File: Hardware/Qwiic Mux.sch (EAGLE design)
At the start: 77 parts, among them J1 SMD, J10 SMD, J11 PTH, J12 PTH, J13 PTH, J14 PTH, J2 SMD, J23 SMD, J24 SMD, J25 SMD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

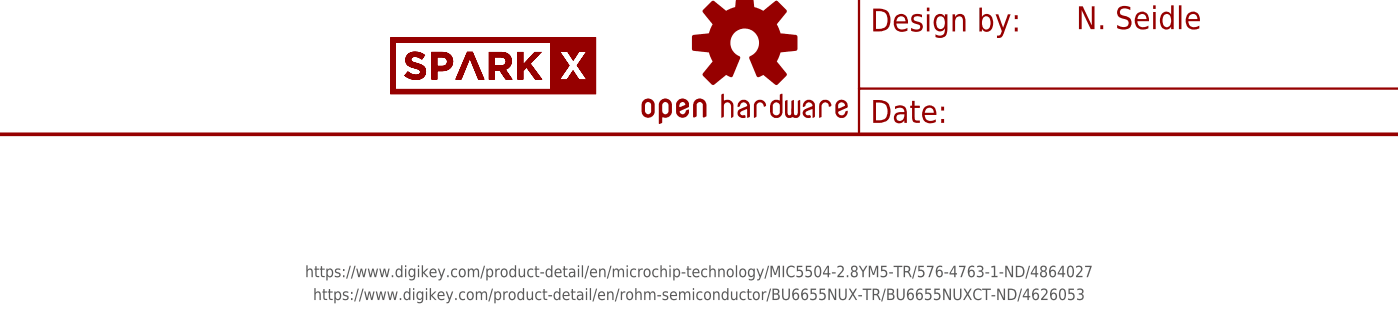
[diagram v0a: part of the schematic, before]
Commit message: Adding example firmware
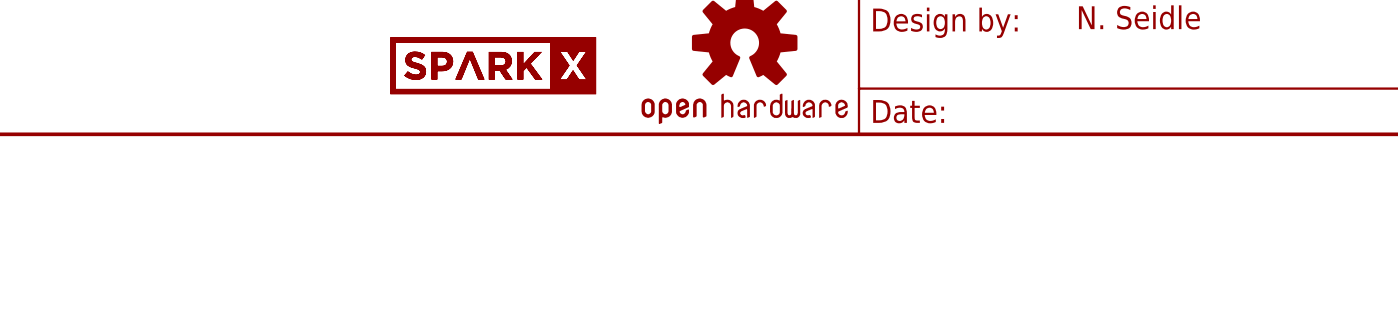
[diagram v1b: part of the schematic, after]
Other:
- note removed: "https://www.digikey.com/product-detail/en/microchip-technology/MIC5504-2.8YM5-TR/576-4763-1-ND/4864027"
- note removed: "https://www.digikey.com/product-detail/en/rohm-semiconductor/BU6655NUX-TR/BU6655NUXCT-ND/4626053"
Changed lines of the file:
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@@
 <text x="467.36" y="99.06" size="3.048" layer="97" font="vector" ratio="12">6: 3.3V Bus</text>
 <text x="467.36" y="127" size="3.048" layer="97" font="vector" ratio="12">7: 3.3V Bus</text>
-<text x="129.54" y="-17.78" size="1.27" layer="97" align="center">https://www.digikey.com/product-detail/en/rohm-semiconductor/BU6655NUX-TR/BU6655NUXCT-ND/4626053</text>
-<text x="129.54" y="-15.24" size="1.27" layer="97" align="center">https://www.digikey.com/product-detail/en/microchip-technology/MIC5504-2.8YM5-TR/576-4763-1-ND/4864027</text>
 <text x="132.08" y="177.8" size="3.048" layer="97" font="vector" ratio="12" align="center">Power</text>
 <text x="66.04" y="149.86" size="1.778" layer="97" align="center">By default 3.3V is provided by master</text>

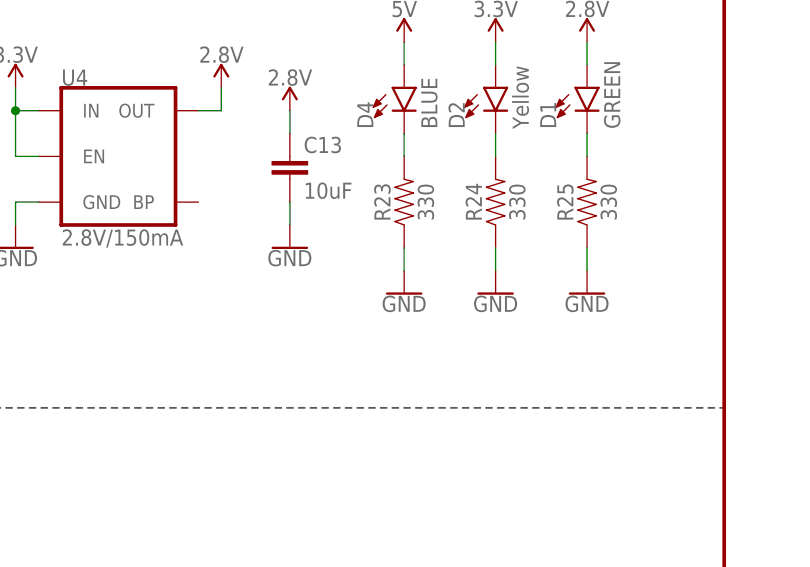
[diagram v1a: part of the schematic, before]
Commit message: Fixing silk. Fixing 5V LED circuit.
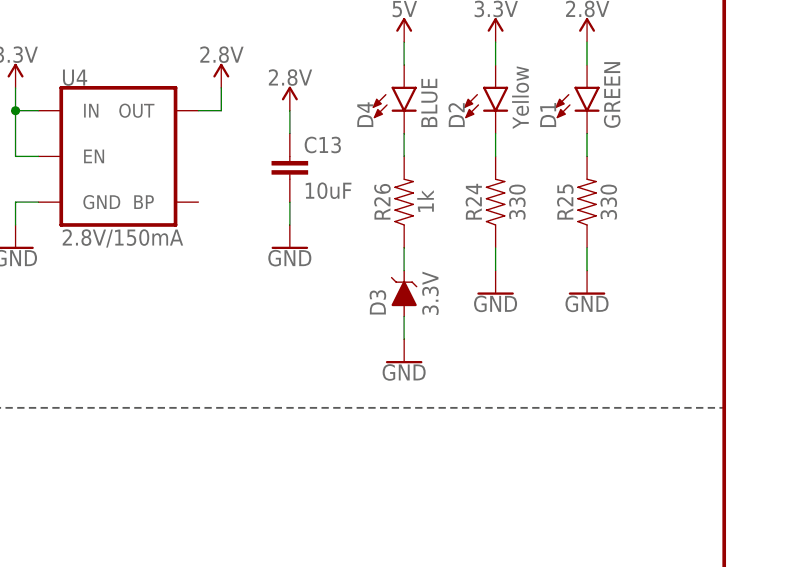
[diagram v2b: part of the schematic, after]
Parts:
- removed R23: 330, SparkFun-Resistors:330OHM-0603-1/10W-1%
- added D3: 3.3V, SparkFun-DiscreteSemi:DIODE-ZENER-MM3Z3V3T1G
- added R26: 1k, SparkFun-Resistors:1KOHM-0603-1/10W-1%
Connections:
- new net N$2: D3.C, R26.1
- net GND: now also D3.A; no longer R23.1
- net N$4: now also R26.2; no longer R23.2
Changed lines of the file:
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@@
 <part name="SUPPLY18" library="SparkFun-PowerSymbols" deviceset="3.3V" device=""/>
 <part name="SUPPLY19" library="SparkFun-PowerSymbols" deviceset="5V" device=""/>
-<part name="R23" library="SparkFun-Resistors" deviceset="330OHM" device="-0603-1/10W-1%" value="330"/>
 <part name="R25" library="SparkFun-Resistors" deviceset="330OHM" device="-0603-1/10W-1%" value="330"/>
 <part name="GND21" library="SparkFun-PowerSymbols" deviceset="GND" device=""/>
@@
 <part name="SUPPLY84" library="SparkFun-PowerSymbols" deviceset="3.3V" device=""/>
 <part name="R24" library="SparkFun-Resistors" deviceset="330OHM" device="-0603-1/10W-1%" value="330"/>
+<part name="R26" library="SparkFun-Resistors" deviceset="1KOHM" device="-0603-1/10W-1%" value="1k"/>
+<part name="D3" library="SparkFun-DiscreteSemi" deviceset="DIODE-ZENER" device="-MM3Z3V3T1G" value="3.3V"/>
 </parts>
 <sheets>
@@
 <instance part="SUPPLY18" gate="G$1" x="223.52" y="170.18"/>
 <instance part="SUPPLY19" gate="G$1" x="213.36" y="170.18"/>
-<instance part="R23" gate="G$1" x="213.36" y="152.4" rot="R90"/>
 <instance part="R25" gate="G$1" x="233.68" y="152.4" rot="R90"/>
-<instance part="GND21" gate="1" x="213.36" y="142.24"/>
+<instance part="GND21" gate="1" x="213.36" y="134.62"/>
 <instance part="GND37" gate="1" x="223.52" y="142.24"/>
 <instance part="GND40" gate="1" x="233.68" y="142.24"/>
@@
 <instance part="SUPPLY84" gate="G$1" x="515.62" y="132.08"/>
 <instance part="R24" gate="G$1" x="223.52" y="152.4" rot="R90"/>
+<instance part="R26" gate="G$1" x="213.36" y="152.4" rot="R90"/>
+<instance part="D3" gate="G$1" x="213.36" y="142.24" rot="R90"/>
 </instances>
 <busses>
@@
 </segment>
 <segment>
-<pinref part="R23" gate="G$1" pin="1"/>
-<pinref part="GND21" gate="1" pin="GND"/>
-<wire x1="213.36" y1="144.78" x2="213.36" y2="147.32" width="0.1524" layer="91"/>
-</segment>
-<segment>
 <pinref part="GND37" gate="1" pin="GND"/>
 <wire x1="223.52" y1="144.78" x2="223.52" y2="147.32" width="0.1524" layer="91"/>
@@
 <pinref part="GND40" gate="1" pin="GND"/>
 <wire x1="233.68" y1="144.78" x2="233.68" y2="147.32" width="0.1524" layer="91"/>
+</segment>
+<segment>
+<pinref part="D3" gate="G$1" pin="A"/>
+<pinref part="GND21" gate="1" pin="GND"/>
+<wire x1="213.36" y1="137.16" x2="213.36" y2="139.7" width="0.1524" layer="91"/>
 </segment>
 </net>
@@
 <segment>
 <pinref part="D4" gate="G$1" pin="C"/>
-<pinref part="R23" gate="G$1" pin="2"/>
 <wire x1="213.36" y1="157.48" x2="213.36" y2="160.02" width="0.1524" layer="91"/>
-</segment>
-</net>
+<pinref part="R26" gate="G$1" pin="2"/>
+</segment>
+</net>
+<net name="N$2" class="0">
+<segment>
+<pinref part="R26" gate="G$1" pin="1"/>
+<pinref part="D3" gate="G$1" pin="C"/>
+<wire x1="213.36" y1="144.78" x2="213.36" y2="147.32" width="0.1524" layer="91"/>
+</segment>
+</net>
